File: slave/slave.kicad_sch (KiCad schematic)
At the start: 0 parts

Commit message: feat(slave): add complete slave board schematic and project configuration
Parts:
- added C_5V1: 100uF, Capacitor_SMD:C_1206_3216Metric, symbol board_game:Capacitor
- added C_5V2, C_ATTINY1: 100nF, Capacitor_SMD:C_0603_1608Metric, symbol board_game:Capacitor
- added C_BULK1: 100uF_25V, Capacitor_SMD:CP_Elec_6.3x7.7, symbol board_game:Capacitor
- added D_TVS1: SMAJ12A, Diode_SMD:D_SMA, symbol board_game:Shunt_Protection
- added J_EAST1: MAG_EAST_6PIN_FEMALE, symbol board_game:Magnetic_6Pin_Female
- added J_NORTH1: MAG_NORTH_6PIN_FEMALE, symbol board_game:Magnetic_6Pin_Female
- added J_SOUTH1: MAG_SOUTH_6PIN_MALE, symbol board_game:Magnetic_6Pin_Male
- added J_UPDI1: UPDI_PROG, Connector_PinHeader_2.54mm:PinHeader_1x03_P2.54mm_Vertical, symbol board_game:UPDI_Header
- added J_WEST1: MAG_WEST_6PIN_MALE, symbol board_game:Magnetic_6Pin_Male
- added MOD1, MOD10, MOD11, MOD12, MOD13, MOD14, MOD15, MOD16, MOD2, MOD3, MOD4, MOD5, MOD6, MOD7, MOD8, MOD9: WS2812_Matrix_2x2, ws2812-matrix-2x2:WS2812_Matrix_2x2_15x15mm, symbol ws2812-matrix-2x2:WS2812_Matrix_2x2
- added R_ED0, R_ED1, R_ND0, R_ND1, R_SD0, R_SD1, R_WD0, R_WD1: 330R, Resistor_SMD:R_0603_1608Metric, symbol board_game:Series_Resistor
- added R_LED1: 470R, Resistor_SMD:R_0603_1608Metric, symbol board_game:Series_Resistor
- added U1: ATtiny1604-SS, Package_SO:SOIC-14_3.9x8.7mm_P1.27mm, symbol MCU_Microchip_ATtiny:ATtiny1604-SS
- added U_BUCK1: MP2315_MINI_5V_3A, Module:MP2315_Mini_StepDown, symbol board_game:MP2315_StepDown
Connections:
- new net: MOD15.6 (VCC_OUT), MOD16.2 (VCC_IN)
- new net: MOD15.7 (DOUT), MOD16.3 (DIN)
- new net: MOD15.8 (GND_OUT2), MOD16.4 (GND_IN2)
- new net: R_ED0.1, U1.2 (PA4)
- new net: R_WD1.1, U1.6 (PB3)
- new net: MOD1.6 (VCC_OUT), MOD2.2 (VCC_IN)
- new net: MOD1.7 (DOUT), MOD2.3 (DIN)
- new net: MOD1.8 (GND_OUT2), MOD2.4 (GND_IN2)
- new net: MOD6.6 (VCC_OUT), MOD7.2 (VCC_IN)
- new net: MOD6.7 (DOUT), MOD7.3 (DIN)
- new net: MOD6.8 (GND_OUT2), MOD7.4 (GND_IN2)
- new net: MOD7.6 (VCC_OUT), MOD8.2 (VCC_IN)
- new net: MOD7.7 (DOUT), MOD8.3 (DIN)
- new net: MOD7.8 (GND_OUT2), MOD8.4 (GND_IN2)
- new net: MOD10.2 (VCC_IN), MOD9.6 (VCC_OUT)
- new net: MOD10.3 (DIN), MOD9.7 (DOUT)
- new net: MOD10.4 (GND_IN2), MOD9.8 (GND_OUT2)
- new net: MOD10.6 (VCC_OUT), MOD11.2 (VCC_IN)
- new net: MOD10.7 (DOUT), MOD11.3 (DIN)
- new net: MOD10.8 (GND_OUT2), MOD11.4 (GND_IN2)
- new net: R_ND0.1, U1.12 (PA2)
- new net: R_SD0.1, U1.4 (PA6)
- new net: MOD2.6 (VCC_OUT), MOD3.2 (VCC_IN)
- new net: MOD2.7 (DOUT), MOD3.3 (DIN)
- new net: MOD2.8 (GND_OUT2), MOD3.4 (GND_IN2)
- new net: MOD3.6 (VCC_OUT), MOD4.2 (VCC_IN)
- new net: MOD3.7 (DOUT), MOD4.3 (DIN)
- new net: MOD3.8 (GND_OUT2), MOD4.4 (GND_IN2)
- new net: R_SD1.1, U1.5 (PA7)
- new net: R_LED1.1, U1.11 (PA1)
- new net: MOD14.6 (VCC_OUT), MOD15.2 (VCC_IN)
- new net: MOD14.7 (DOUT), MOD15.3 (DIN)
- new net: MOD14.8 (GND_OUT2), MOD15.4 (GND_IN2)
- new net: R_ED1.1, U1.3 (PA5)
- new net: R_WD0.1, U1.7 (PB2)
- new net: R_ND1.1, U1.13 (PA3)
- new net: MOD5.6 (VCC_OUT), MOD6.2 (VCC_IN)
- new net: MOD5.7 (DOUT), MOD6.3 (DIN)
- new net: MOD5.8 (GND_OUT2), MOD6.4 (GND_IN2)
- new net: MOD11.6 (VCC_OUT), MOD12.2 (VCC_IN)
- new net: MOD11.7 (DOUT), MOD12.3 (DIN)
- new net: MOD11.8 (GND_OUT2), MOD12.4 (GND_IN2)
- new net: MOD13.6 (VCC_OUT), MOD14.2 (VCC_IN)
- new net: MOD13.7 (DOUT), MOD14.3 (DIN)
- new net: MOD13.8 (GND_OUT2), MOD14.4 (GND_IN2)
- new net +12V_BUS: C_BULK1.1, D_TVS1.1 (5V), J_EAST1.1 (5V_1), J_EAST1.6 (5V_2), J_NORTH1.1 (5V_1), J_NORTH1.6 (5V_2), J_SOUTH1.1 (5V_1), J_SOUTH1.6 (5V_2), J_WEST1.1 (5V_1), J_WEST1.6 (5V_2), U_BUCK1.1 (IN+)
- new net +5V_LOCAL: C_5V1.1, C_5V2.1, C_ATTINY1.1, J_UPDI1.1 (+5V), MOD1.2 (VCC_IN), MOD13.2 (VCC_IN), MOD5.2 (VCC_IN), MOD9.2 (VCC_IN), U1.1 (VCC), U_BUCK1.3 (OUT+)
- new net E_D0: J_EAST1.3 (D0), R_ED0.2
- new net E_D1: J_EAST1.4 (D1), R_ED1.2
- new net GND: C_5V1.2, C_5V2.2, C_ATTINY1.2, C_BULK1.2, D_TVS1.2 (GND), J_EAST1.2 (GND_1), J_EAST1.5 (GND_2), J_NORTH1.2 (GND_1), J_NORTH1.5 (GND_2), J_SOUTH1.2 (GND_1), J_SOUTH1.5 (GND_2), J_UPDI1.3 (GND), J_WEST1.2 (GND_1), J_WEST1.5 (GND_2), MOD1.4 (GND_IN2), MOD13.4 (GND_IN2), MOD5.4 (GND_IN2), MOD9.4 (GND_IN2), U1.14 (GND), U_BUCK1.2 (IN-), U_BUCK1.4 (OUT-)
- new net LED_DIN: MOD1.3 (DIN), R_LED1.2
- new net LED_R1_TO_R2: MOD4.7 (DOUT), MOD5.3 (DIN)
- new net LED_R2_TO_R3: MOD8.7 (DOUT), MOD9.3 (DIN)
- new net LED_R3_TO_R4: MOD12.7 (DOUT), MOD13.3 (DIN)
- new net N_D0: J_NORTH1.3 (D0), R_ND0.2
- new net N_D1: J_NORTH1.4 (D1), R_ND1.2
- new net S_D0: J_SOUTH1.4 (D0), R_SD0.2
- new net S_D1: J_SOUTH1.3 (D1), R_SD1.2
- new net UPDI: J_UPDI1.2 (UPDI), U1.10 (~{RESET}/PA0)
- new net W_D0: J_WEST1.4 (D0), R_WD0.2
- new net W_D1: J_WEST1.3 (D1), R_WD1.2
- no-connect marks 0 -> 43
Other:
- note added: "1. TILE CONTROLLER (ATTINY1604) & INTERFACES"
- note added: "2. 12V BUS INPUT, PROTECTION & 5V 3A STEP-DOWN"
- note added: "3. 6-PIN MAGNETIC EDGE CONNECTORS: NORTH, EAST, SOUTH, WEST"
- note added: "4. SMART LED MATRIX 4x4 (64 LEDs): WS2812 2x2 DAISY-CHAIN"

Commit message: feat(slave): export schematic to PDF and resolve ERC violations
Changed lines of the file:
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@@
 	(no_connect (at 25.4 120.65))
 	(no_connect (at 25.4 123.19))
-	(wire (pts (xy 25.4 125.73) (xy 25.4 105.41)) (stroke (width 0) (type default)))
-	(wire (pts (xy 25.4 105.41) (xy 45.72 105.41)) (stroke (width 0) (type default)))
+	(wire (pts (xy 25.4 125.73) (xy 20.32 125.73)) (stroke (width 0) (type default)))
+	(wire (pts (xy 20.32 125.73) (xy 20.32 105.41)) (stroke (width 0) (type default)))
+	(wire (pts (xy 20.32 105.41) (xy 45.72 105.41)) (stroke (width 0) (type default)))
 	(symbol
 		(lib_id "board_game:Series_Resistor")
@@
 		)
 	)
-	(wire (pts (xy 25.4 128.27) (xy 22.86 128.27)) (stroke (width 0) (type default)))
-	(wire (pts (xy 22.86 128.27) (xy 22.86 95.25)) (stroke (width 0) (type default)))
-	(wire (pts (xy 22.86 95.25) (xy 66.04 95.25)) (stroke (width 0) (type default)))
+	(wire (pts (xy 25.4 128.27) (xy 17.78 128.27)) (stroke (width 0) (type default)))
+	(wire (pts (xy 17.78 128.27) (xy 17.78 95.25)) (stroke (width 0) (type default)))
+	(wire (pts (xy 17.78 95.25) (xy 66.04 95.25)) (stroke (width 0) (type default)))
 	(symbol
 		(lib_id "board_game:Series_Resistor")
@@
 		)
 	)
-	(wire (pts (xy 35.56 204.47) (xy 76.2 204.47)) (stroke (width 0) (type default)))
+	(wire (pts (xy 35.56 204.47) (xy 66.04 204.47)) (stroke (width 0) (type default)))
 	(global_label "+12V_BUS"
 		(shape input)
@@
 				(font
 					(size 1.27 1.27)
+				)
+			)
+		)
+	)
+	(junction (at 35.56 204.47) (diameter 1.016) (color 0 0 0 0))
+	(wire (pts (xy 35.56 204.47) (xy 35.56 195.58)) (stroke (width 0) (type default)))
+	(symbol
+		(lib_id "power:PWR_FLAG")
+		(at 35.56 195.58 0)
+		(unit 1)
+		(body_style 1)
+		(exclude_from_sim no)
+		(in_bom yes)
+		(on_board yes)
+		(in_pos_files yes)
+		(dnp no)
+		(property "Reference" "#PWR01"
+			(at 35.56 191.77 0)
+			(show_name no)
+			(do_not_autoplace no)
+			(effects (font (size 1.27 1.27)))
+		)
+		(property "Value" "PWR_FLAG"
+			(at 35.56 190.5 0)
+			(show_name no)
+			(do_not_autoplace no)
+			(effects (font (size 1.27 1.27)))
+		)
+		(property "Footprint" ""
+			(at 35.56 195.58 0)
+			(hide yes)
+			(show_name no)
+			(do_not_autoplace no)
+			(effects (font (size 1.27 1.27)))
+		)
+		(property "Datasheet" "~"
+			(at 35.56 195.58 0)
+			(hide yes)
+			(show_name no)
+			(do_not_autoplace no)
+			(effects (font (size 1.27 1.27)))
+		)
+		(property "Description" "Power flag"
+			(at 35.56 195.58 0)
+			(hide yes)
+			(show_name no)
+			(do_not_autoplace no)
+			(effects (font (size 1.27 1.27)))
+		)
+		(pin "1")
+		(instances
+			(project "slave"
+				(path "/6535a50c-711e-40d0-ab15-815f580a5cbd"
+					(reference "#PWR01")
+					(unit 1)
 				)
 			)
@@
 		)
 	)
-	(junction (at 66.04 204.47) (diameter 1.016) (color 0 0 0 0))
 	(wire (pts (xy 66.04 204.47) (xy 66.04 208.28)) (stroke (width 0) (type default)))
 	(symbol
@@
 				(font
 					(size 1.27 1.27)
+				)
+			)
+		)
+	)
+	(junction (at 66.04 218.44) (diameter 1.016) (color 0 0 0 0))
+	(wire (pts (xy 66.04 218.44) (xy 66.04 226.06)) (stroke (width 0) (type default)))
+	(symbol
+		(lib_id "power:PWR_FLAG")
+		(at 66.04 226.06 0)
+		(unit 1)
+		(body_style 1)
+		(exclude_from_sim no)
+		(in_bom yes)
+		(on_board yes)
+		(in_pos_files yes)
+		(dnp no)
+		(property "Reference" "#PWR02"
+			(at 66.04 229.87 0)
+			(show_name no)
+			(do_not_autoplace no)
+			(effects (font (size 1.27 1.27)))
+		)
+		(property "Value" "PWR_FLAG"
+			(at 66.04 231.14 0)
+			(show_name no)
+			(do_not_autoplace no)
+			(effects (font (size 1.27 1.27)))
+		)
+		(property "Footprint" ""
+			(at 66.04 226.06 0)
+			(hide yes)
+			(show_name no)
+			(do_not_autoplace no)
+			(effects (font (size 1.27 1.27)))
+		)
+		(property "Datasheet" "~"
+			(at 66.04 226.06 0)
+			(hide yes)
+			(show_name no)
+			(do_not_autoplace no)
+			(effects (font (size 1.27 1.27)))
+		)
+		(property "Description" "Power flag"
+			(at 66.04 226.06 0)
+			(hide yes)
+			(show_name no)
+			(do_not_autoplace no)
+			(effects (font (size 1.27 1.27)))
+		)
+		(pin "1")
+		(instances
+			(project "slave"
+				(path "/6535a50c-711e-40d0-ab15-815f580a5cbd"
+					(reference "#PWR02")
+					(unit 1)
 				)
 			)
@@
 				)
 			)
-		)
-	)
-	(junction (at 109.22 251.46) (diameter 1.016) (color 0 0 0 0))
-	(wire (pts (xy 109.22 251.46) (xy 109.22 245)) (stroke (width 0) (type default)))
-	(symbol
-		(lib_id "power:PWR_FLAG")
-		(at 109.22 245 0)
-		(unit 1)
-		(body_style 1)
-		(exclude_from_sim no)
-		(in_bom yes)
-		(on_board yes)
-		(in_pos_files yes)
-		(dnp no)
-		(property "Reference" "#PWR01"
-			(at 109.22 241.19 0)
-			(show_name no)
-			(do_not_autoplace no)
-			(effects (font (size 1.27 1.27)))
-		)
-		(property "Value" "PWR_FLAG"
-			(at 109.22 239.92 0)
-			(show_name no)
-			(do_not_autoplace no)
-			(effects (font (size 1.27 1.27)))
-		)
-		(property "Footprint" ""
-			(at 109.22 245 0)
-			(hide yes)
-			(show_name no)
-			(do_not_autoplace no)
-			(effects (font (size 1.27 1.27)))
-		)
-		(property "Datasheet" "~"
-			(at 109.22 245 0)
-			(hide yes)
-			(show_name no)
-			(do_not_autoplace no)
-			(effects (font (size 1.27 1.27)))
-		)
-		(property "Description" "Power flag"
-			(at 109.22 245 0)
-			(hide yes)
-			(show_name no)
-			(do_not_autoplace no)
-			(effects (font (size 1.27 1.27)))
-		)
-		(pin "1")
-		(instances
-			(project "slave"
-				(path "/6535a50c-711e-40d0-ab15-815f580a5cbd"
-					(reference "#PWR01")
-					(unit 1)
-				)
-			)

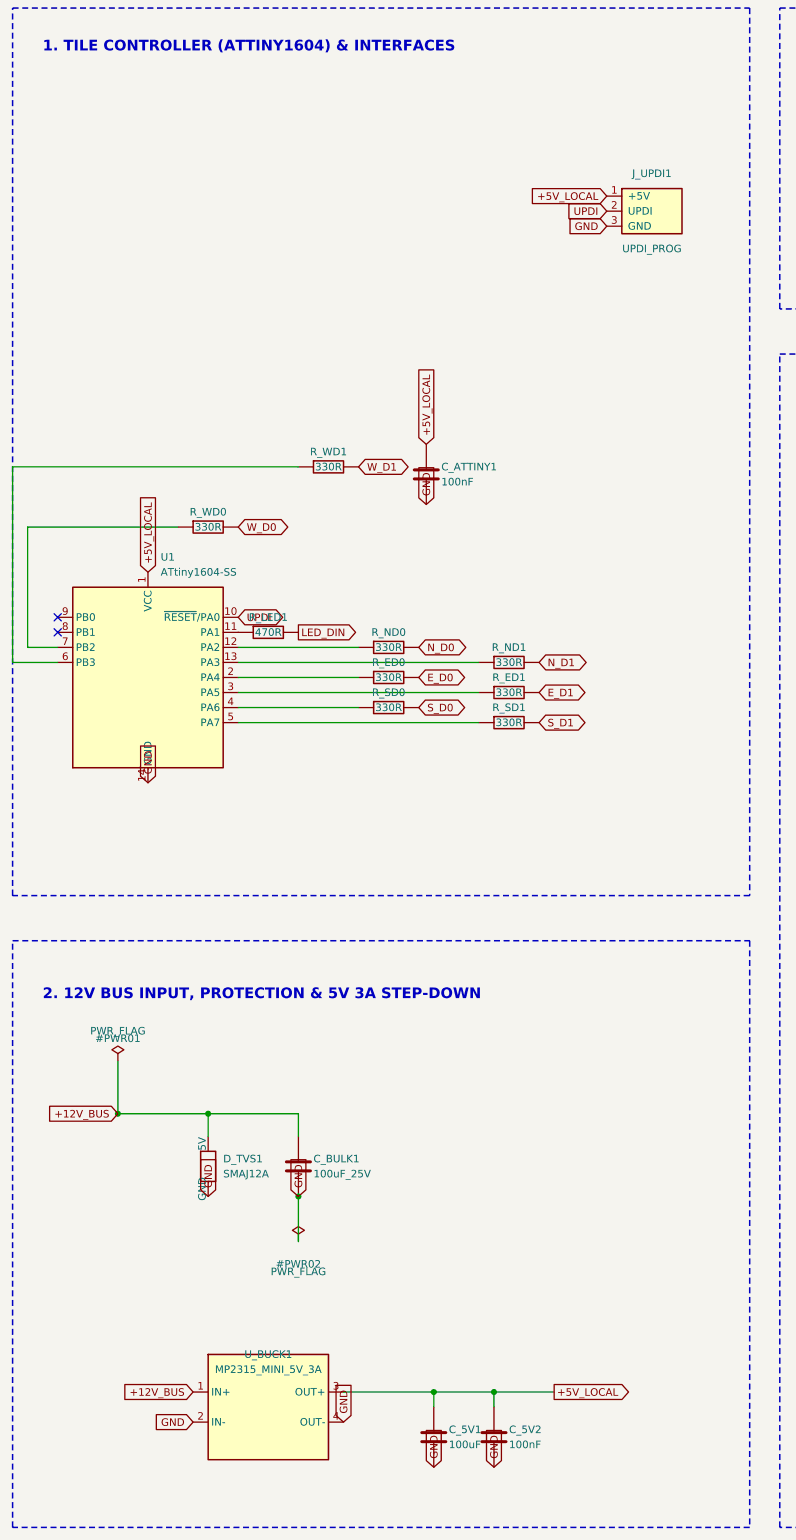
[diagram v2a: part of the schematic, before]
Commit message: chore(slave): update schematic and re-export slave.pdf
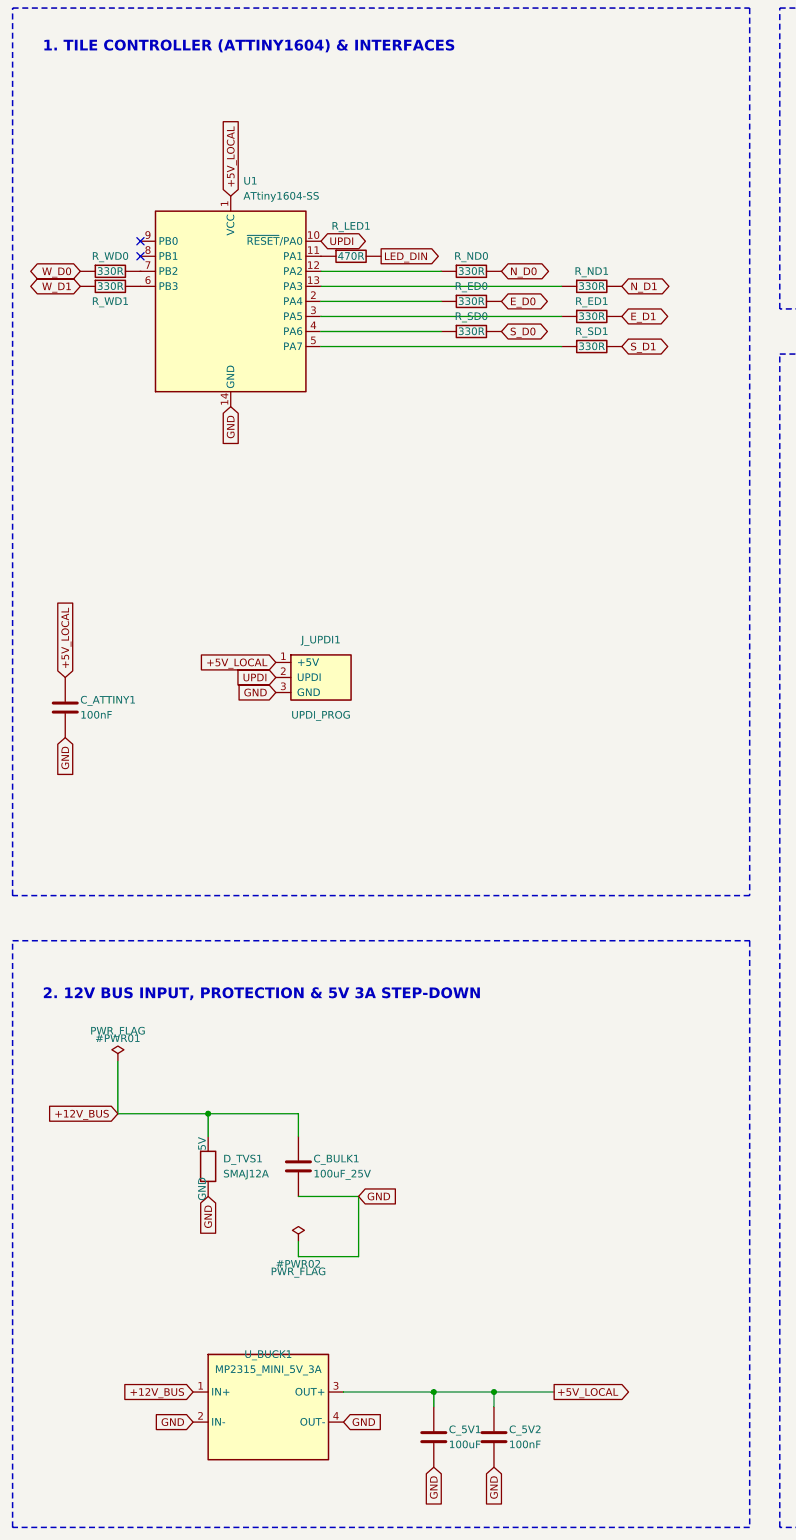
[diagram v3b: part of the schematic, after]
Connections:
- net W_D0: now also R_WD0.1; no longer R_WD0.2
- net W_D1: now also R_WD1.1; no longer R_WD1.2
- net at U1.6 (PB3): now also R_WD1.2; no longer R_WD1.1
- net at U1.7 (PB2): now also R_WD0.2; no longer R_WD0.1
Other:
- moved on the sheet: C_ATTINY1, J_UPDI1, R_ED0, R_ED1, R_LED1, R_ND0, R_ND1, R_SD0, R_SD1, R_WD0, R_WD1, U1
